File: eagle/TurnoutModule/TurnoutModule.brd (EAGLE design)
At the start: 61 x 48.3 mm, 19 parts, among them IC1 L293D, IC2 MCP23008/P

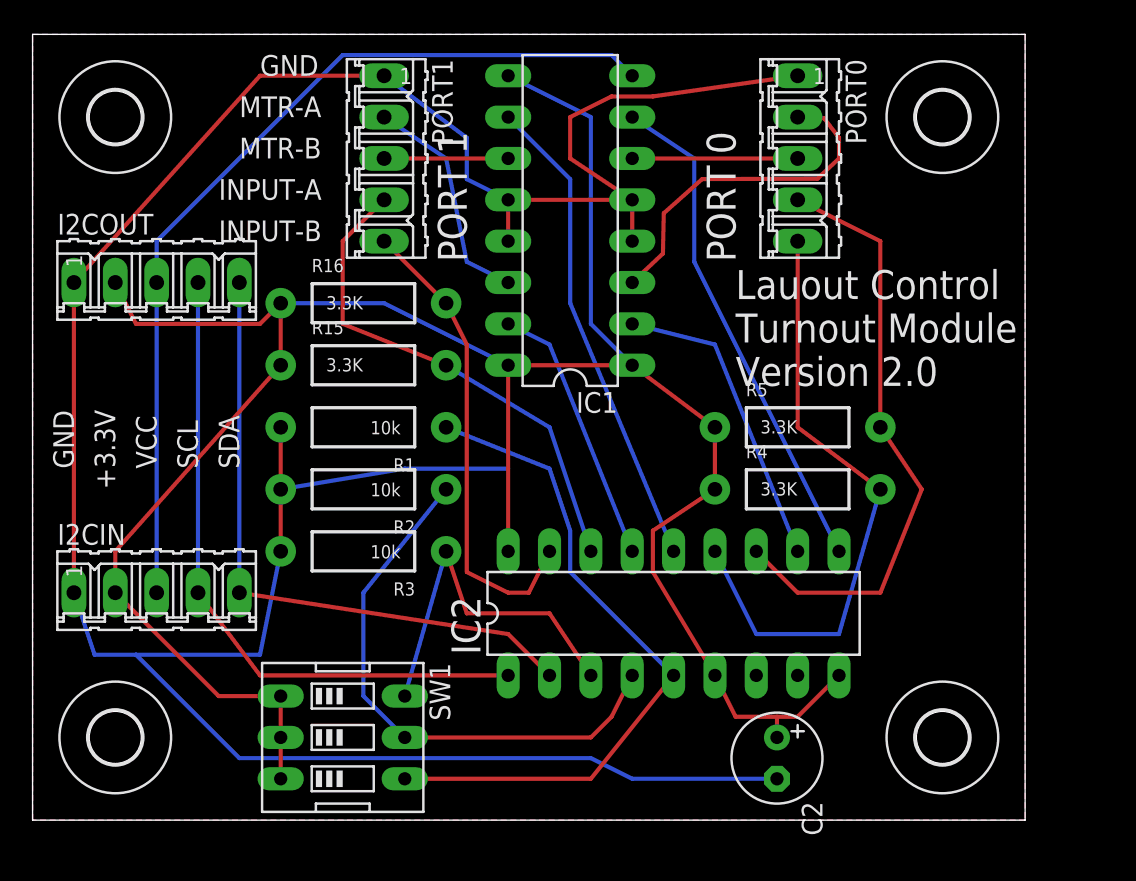
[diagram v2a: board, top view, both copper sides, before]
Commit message: 1.  Add copyDevice to API 2.  Add modelChanged property to JSonModel
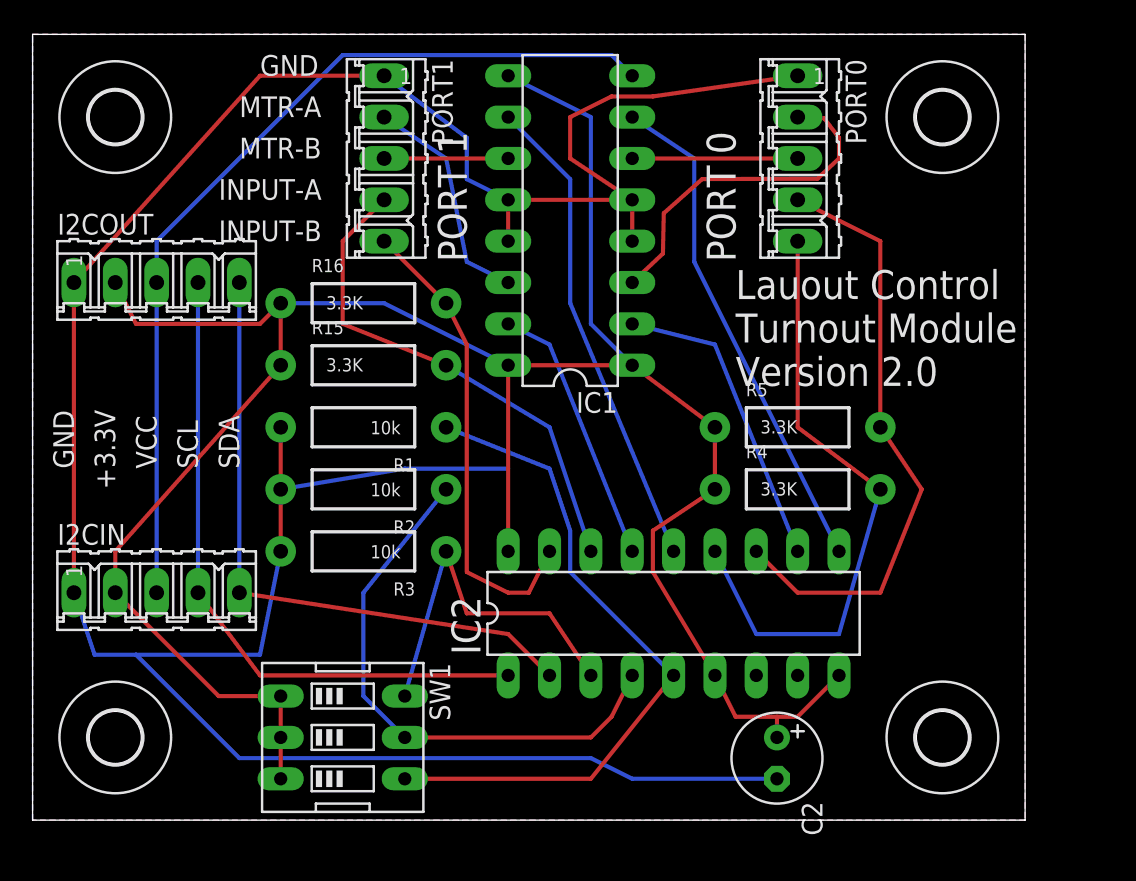
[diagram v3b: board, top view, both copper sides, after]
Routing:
- added copper zone on layer 16, net N$11
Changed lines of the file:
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@@
 <wire x1="22.86" y1="7.62" x2="25.4" y2="16.51" width="0.254" layer="16"/>
+</signal>
+<signal name="N$11">
+<polygon width="0.254" layer="16" isolate="0.3048">
+<vertex x="0" y="0"/>
+<vertex x="0" y="48.26"/>
+<vertex x="60.96" y="48.26"/>
+<vertex x="60.96" y="0"/>
+</polygon>
 </signal>
 </signals>

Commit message: 1.  More adjustments to block detector 2.  Expander8 and Expander16 classes now impose a retry count.  More than three failed read/write attempts causes the module to be disabled. 3.  Signals now allow for both AND and OR conditions 4.  Fix TurnoutModule schematic and board layout for missing ground on expander chip 5.  NetworkManager now also detects WL_CONNECTION_LOST condition 6.  Database SignalCondition table updated with new conditionType field. 7.  Version change to 3.0.21
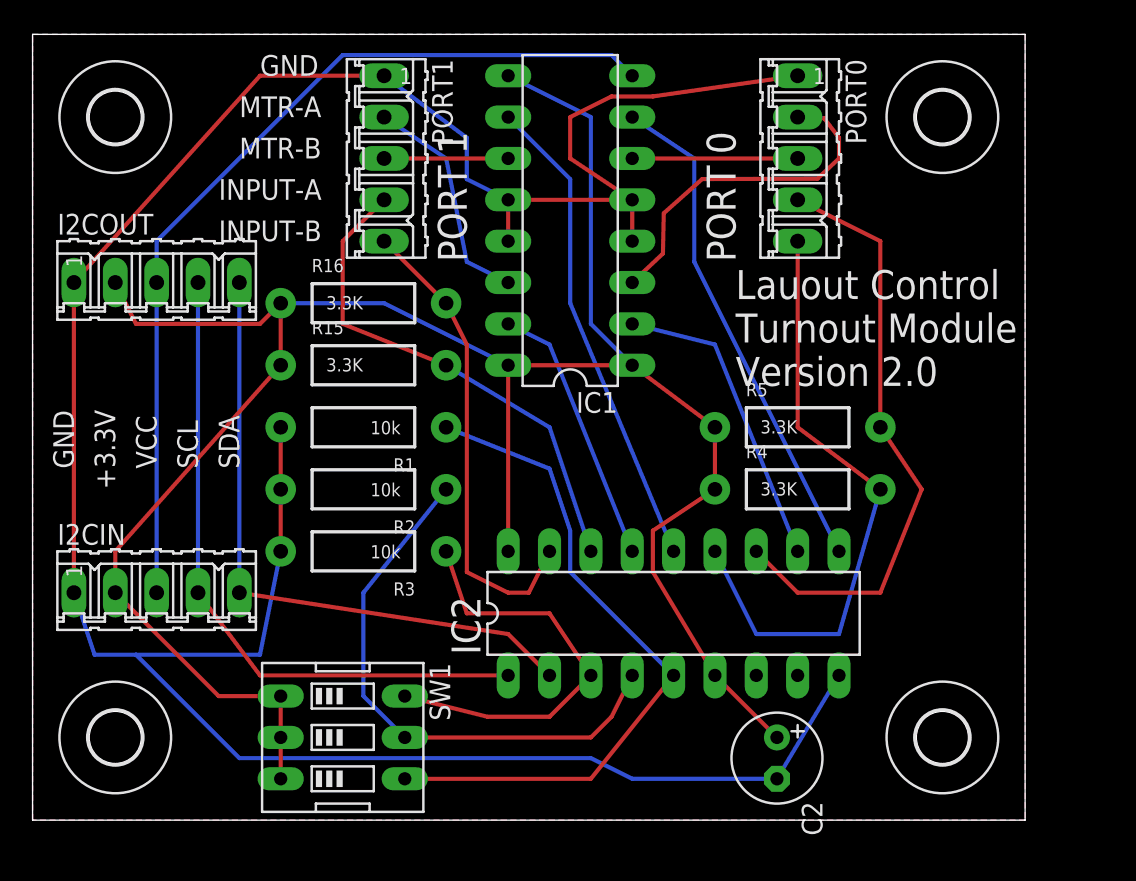
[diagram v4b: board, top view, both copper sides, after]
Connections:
- net +3V3: no longer IC2.9
- net GND: now also IC2.9
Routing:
- net GND: track 174.3 -> 167.6 mm
- net +3V3: track 143.9 -> 137.7 mm
- net N$7: track 22.9 -> 26.3 mm
- removed copper zone on layer 16, net N$11
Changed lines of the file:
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@@
 <wire x1="6.35" y1="10.16" x2="3.81" y2="10.16" width="0.254" layer="16"/>
 <wire x1="3.81" y1="10.16" x2="2.54" y2="13.97" width="0.254" layer="16"/>
-<wire x1="15.24" y1="20.32" x2="22.86" y2="21.59" width="0.254" layer="16"/>
-<wire x1="22.86" y1="21.59" x2="29.21" y2="21.59" width="0.254" layer="16"/>
+<contactref element="C2" pad="-"/>
+<wire x1="45.72" y1="2.54" x2="36.83" y2="2.54" width="0.254" layer="16"/>
+<wire x1="36.83" y1="2.54" x2="34.29" y2="3.81" width="0.254" layer="16"/>
+<wire x1="34.29" y1="3.81" x2="12.7" y2="3.81" width="0.254" layer="16"/>
+<wire x1="12.7" y1="3.81" x2="6.35" y2="10.16" width="0.254" layer="16"/>
+<contactref element="IC2" pad="9"/>
+<wire x1="45.72" y1="2.54" x2="49.53" y2="8.89" width="0.254" layer="16"/>
 <polygon width="0.254" layer="1" isolate="0.3048">
 <vertex x="0" y="0"/>
@@
 <vertex x="60.96" y="0"/>
 </polygon>
-<contactref element="C2" pad="-"/>
-<wire x1="45.72" y1="2.54" x2="36.83" y2="2.54" width="0.254" layer="16"/>
-<wire x1="36.83" y1="2.54" x2="34.29" y2="3.81" width="0.254" layer="16"/>
-<wire x1="34.29" y1="3.81" x2="12.7" y2="3.81" width="0.254" layer="16"/>
-<wire x1="12.7" y1="3.81" x2="6.35" y2="10.16" width="0.254" layer="16"/>
 </signal>
 <signal name="N$29">
@@
 <wire x1="13.97" y1="30.48" x2="6.35" y2="30.48" width="0.254" layer="1"/>
 <wire x1="6.35" y1="30.48" x2="5.08" y2="33.02" width="0.254" layer="1"/>
-<contactref element="IC2" pad="9"/>
 <contactref element="SW1" pad="3"/>
 <contactref element="SW1" pad="2"/>
@@
 <wire x1="15.24" y1="7.62" x2="11.43" y2="7.62" width="0.254" layer="1"/>
 <wire x1="11.43" y1="7.62" x2="5.08" y2="13.97" width="0.254" layer="1"/>
-<wire x1="41.91" y1="8.89" x2="43.18" y2="6.35" width="0.254" layer="1"/>
-<wire x1="43.18" y1="6.35" x2="45.72" y2="6.35" width="0.254" layer="1"/>
-<wire x1="45.72" y1="6.35" x2="46.99" y2="6.35" width="0.254" layer="1"/>
-<wire x1="46.99" y1="6.35" x2="49.53" y2="8.89" width="0.254" layer="1"/>
 <contactref element="C2" pad="+"/>
-<wire x1="45.72" y1="5.08" x2="45.72" y2="6.35" width="0.254" layer="1"/>
+<wire x1="45.72" y1="5.08" x2="41.91" y2="8.89" width="0.254" layer="1"/>
 </signal>
 <signal name="N$8">
@@
 <wire x1="26.67" y1="12.7" x2="25.4" y2="16.51" width="0.254" layer="1"/>
 <contactref element="SW1" pad="6"/>
-<wire x1="22.86" y1="7.62" x2="25.4" y2="16.51" width="0.254" layer="16"/>
-</signal>
-<signal name="N$11">
-<polygon width="0.254" layer="16" isolate="0.3048">
-<vertex x="0" y="0"/>
-<vertex x="0" y="48.26"/>
-<vertex x="60.96" y="48.26"/>
-<vertex x="60.96" y="0"/>
-</polygon>
+<wire x1="22.86" y1="7.62" x2="27.94" y2="6.35" width="0.254" layer="1"/>
+<wire x1="27.94" y1="6.35" x2="31.75" y2="6.35" width="0.254" layer="1"/>
+<wire x1="31.75" y1="6.35" x2="34.29" y2="8.89" width="0.254" layer="1"/>
 </signal>
 </signals>
